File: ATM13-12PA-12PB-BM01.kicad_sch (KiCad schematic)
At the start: 1 part

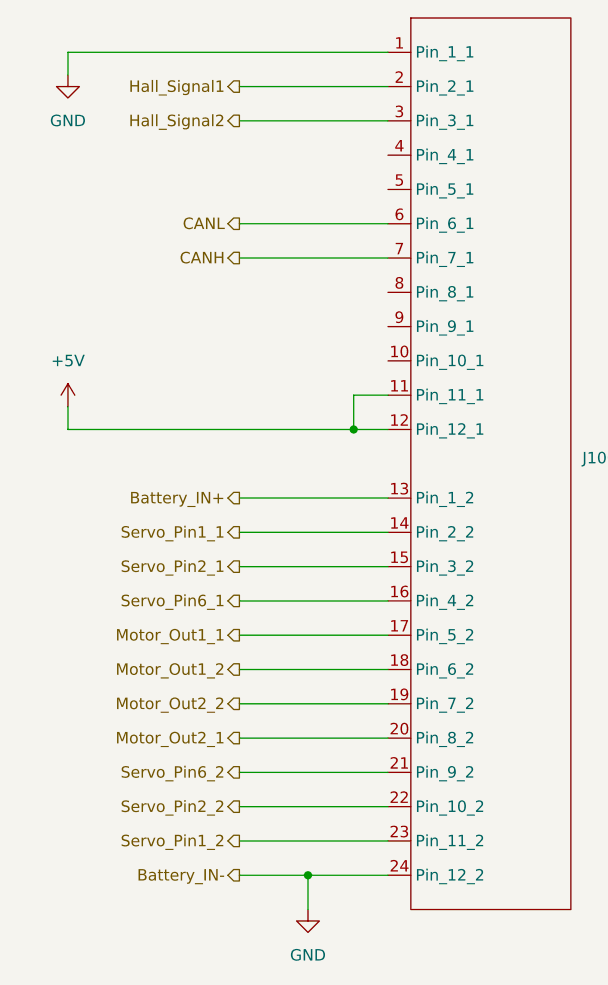
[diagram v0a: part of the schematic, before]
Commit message: Added gyro, current sense, removed servo control, added temp sense
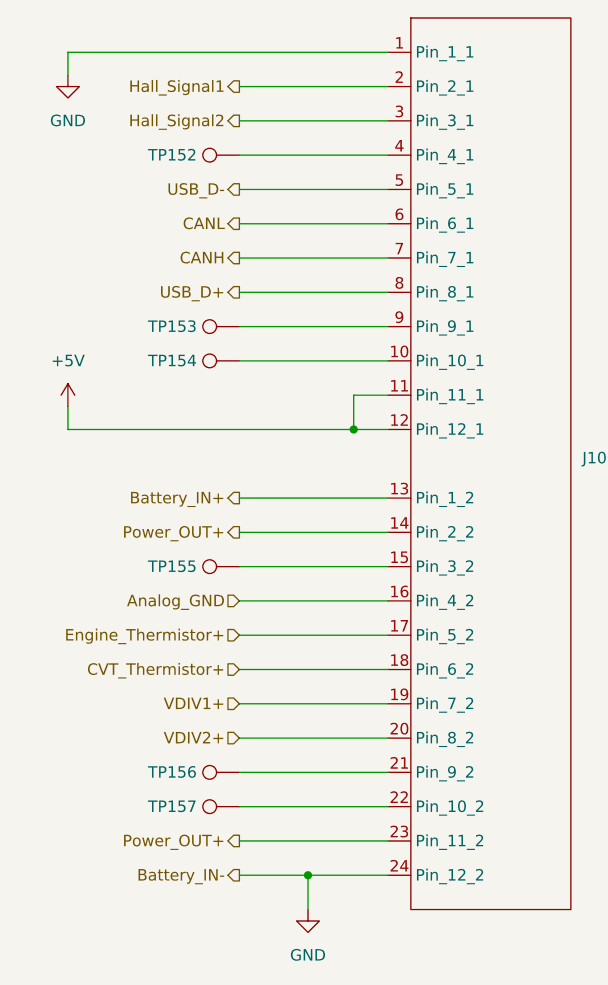
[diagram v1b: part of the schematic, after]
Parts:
- added TP152, TP153, TP154, TP155, TP156, TP157: TestPoint, TestPoint:TestPoint_Pad_D2.0mm, symbol Connector:TestPoint
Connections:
- net Servo_Pin1_2 is gone; now on net Power_OUT+: J100.23 (Pin_11_2)
- net at J100.10 (Pin_10_1): now also TP154.1
- net at J100.4 (Pin_4_1): now also TP152.1
- net USB_D-: now reaches J100.5 (Pin_5_1)
- net USB_D+: now reaches J100.8 (Pin_8_1)
- net at J100.9 (Pin_9_1): now also TP153.1
- net Motor_Out1_1 renamed Engine_Thermistor+
- net Motor_Out1_2 renamed CVT_Thermistor+
- net Motor_Out2_1 renamed VDIV2+
- net Motor_Out2_2 renamed VDIV1+
- net Servo_Pin1_1 renamed Power_OUT+
- net Servo_Pin2_1: no longer names the net of J100.15 (Pin_3_2)
- net Servo_Pin2_1: now also TP155.1
- net Servo_Pin2_2: no longer names the net of J100.22 (Pin_10_2)
- net Servo_Pin2_2: now also TP157.1
- net Servo_Pin6_1 renamed Analog_GND
- net Servo_Pin6_2: no longer names the net of J100.21 (Pin_9_2)
- net Servo_Pin6_2: now also TP156.1

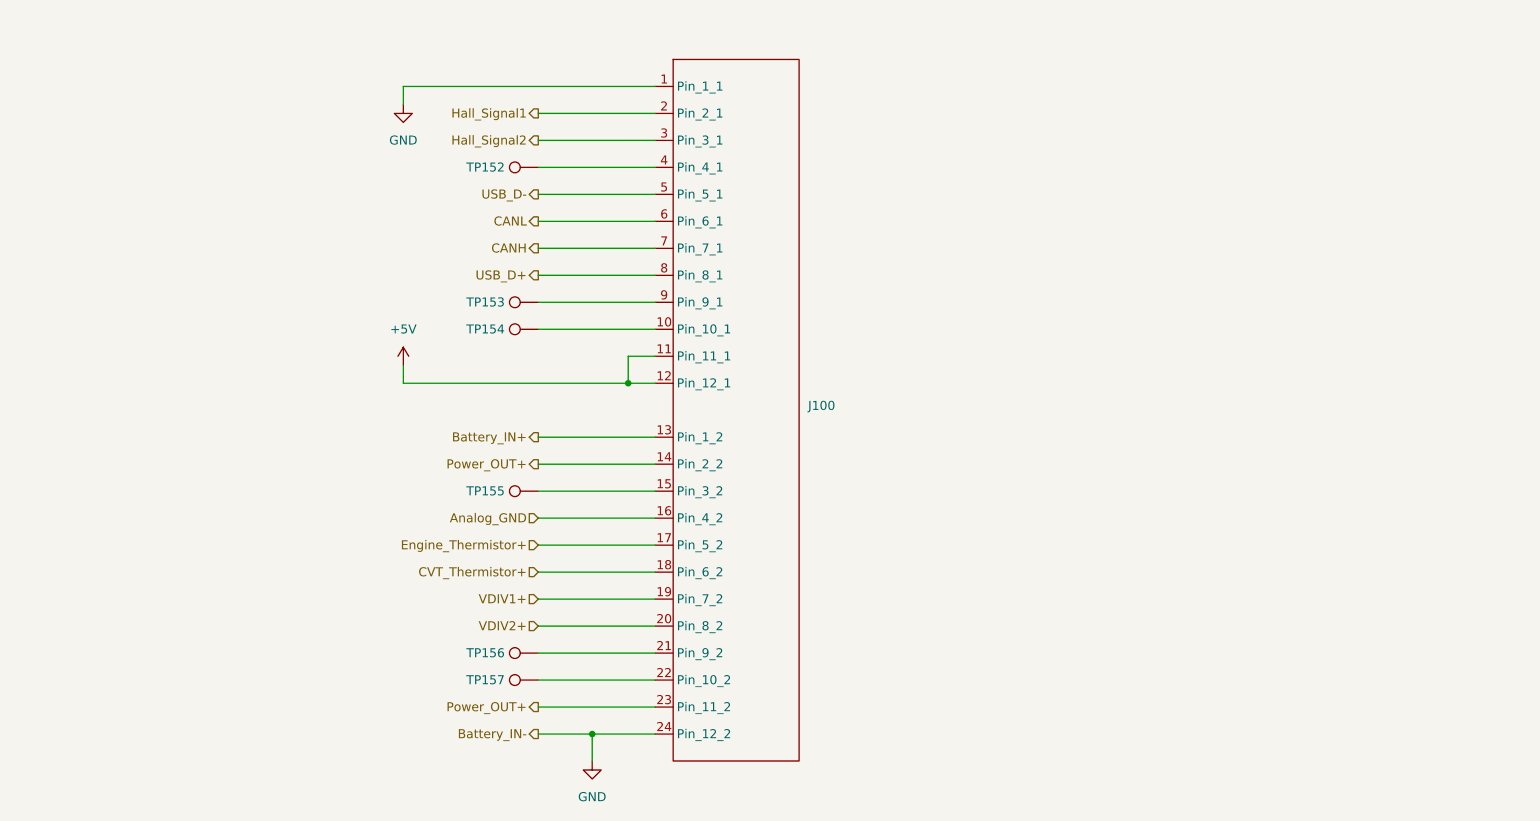
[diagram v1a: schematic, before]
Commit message: finished up schematic, added magnetic sensor, cleaned up pins, etc.
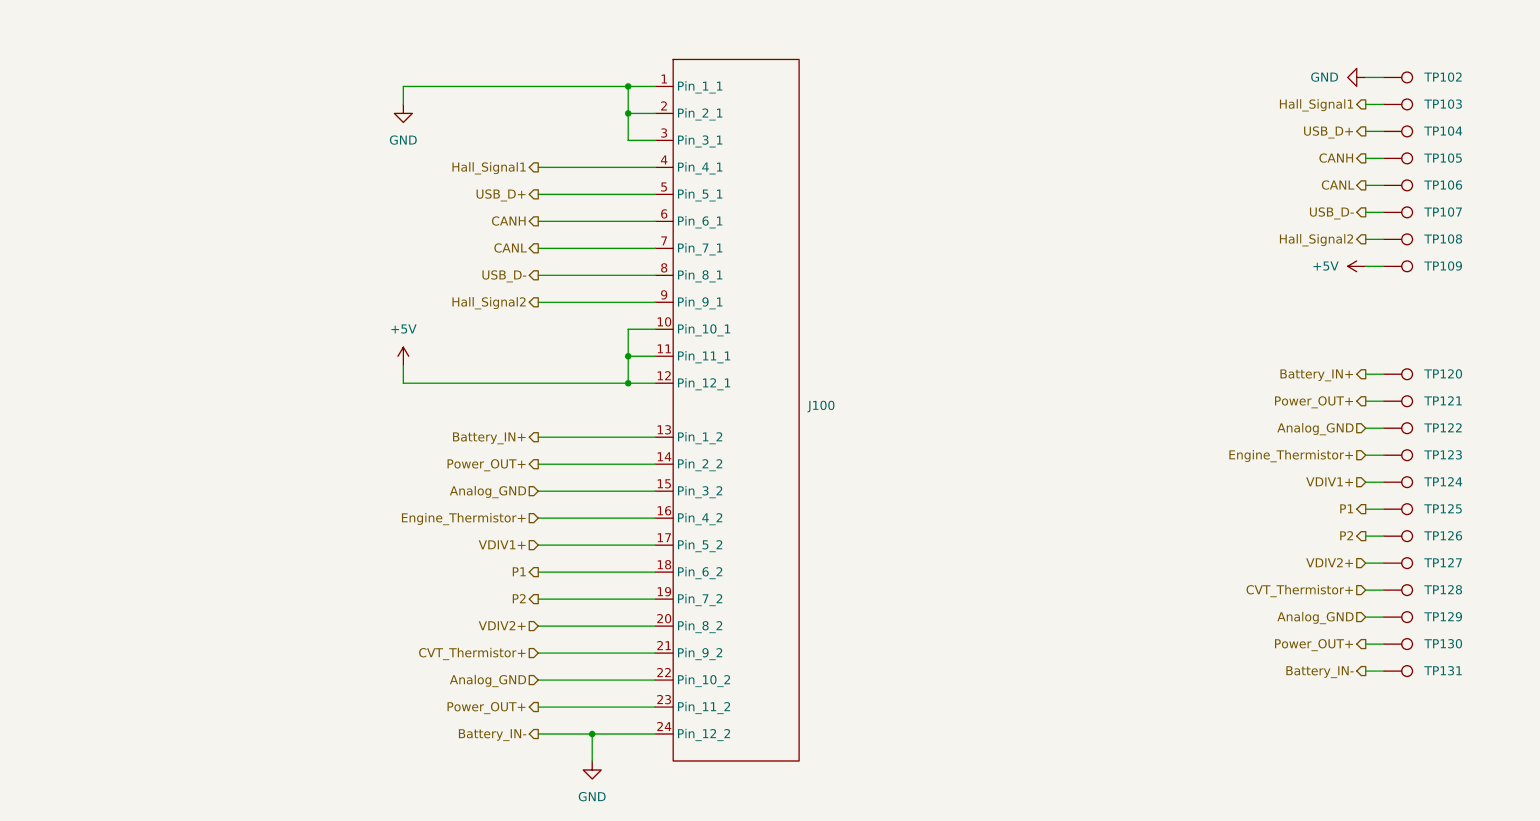
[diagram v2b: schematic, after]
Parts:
- removed TP152, TP153, TP154, TP155, TP156, TP157: TestPoint, TestPoint:TestPoint_Pad_D2.0mm, symbol Connector:TestPoint
- added TP102, TP103, TP104, TP105, TP106, TP107, TP108, TP109, TP120, TP121, TP122, TP123, TP124, TP125, TP126, TP127, TP128, TP129, TP130, TP131: TestPoint, TestPoint:TestPoint_Pad_D1.0mm, symbol Connector:TestPoint
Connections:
- net +5V: now also J100.10 (Pin_10_1), TP109.1
- net Analog_GND: now also J100.15 (Pin_3_2), J100.22 (Pin_10_2), TP122.1, TP129.1; no longer J100.16 (Pin_4_2)
- net Battery_IN+: now also TP120.1
- net CANH: now also J100.6 (Pin_6_1), TP105.1; no longer J100.7 (Pin_7_1)
- net CANL: now also J100.7 (Pin_7_1), TP106.1; no longer J100.6 (Pin_6_1)
- net CVT_Thermistor+: now also J100.21 (Pin_9_2), TP128.1; no longer J100.18 (Pin_6_2)
- net Engine_Thermistor+: now also J100.16 (Pin_4_2), TP123.1; no longer J100.17 (Pin_5_2)
- net GND: now also J100.2 (Pin_2_1), J100.3 (Pin_3_1), TP102.1, TP131.1
- net Hall_Signal1: now also J100.4 (Pin_4_1), TP103.1; no longer J100.2 (Pin_2_1)
- net Hall_Signal2: now also J100.9 (Pin_9_1), TP108.1; no longer J100.3 (Pin_3_1)
- net Power_OUT+: now also TP121.1, TP130.1
- net USB_D+: now also J100.5 (Pin_5_1), TP104.1; no longer J100.8 (Pin_8_1)
- net USB_D-: now also J100.8 (Pin_8_1), TP107.1; no longer J100.5 (Pin_5_1)
- net VDIV1+: now also J100.17 (Pin_5_2), TP124.1; no longer J100.19 (Pin_7_2)
- net VDIV2+: now also TP127.1
- new net P1: J100.18 (Pin_6_2), TP125.1
- new net P2: J100.19 (Pin_7_2), TP126.1

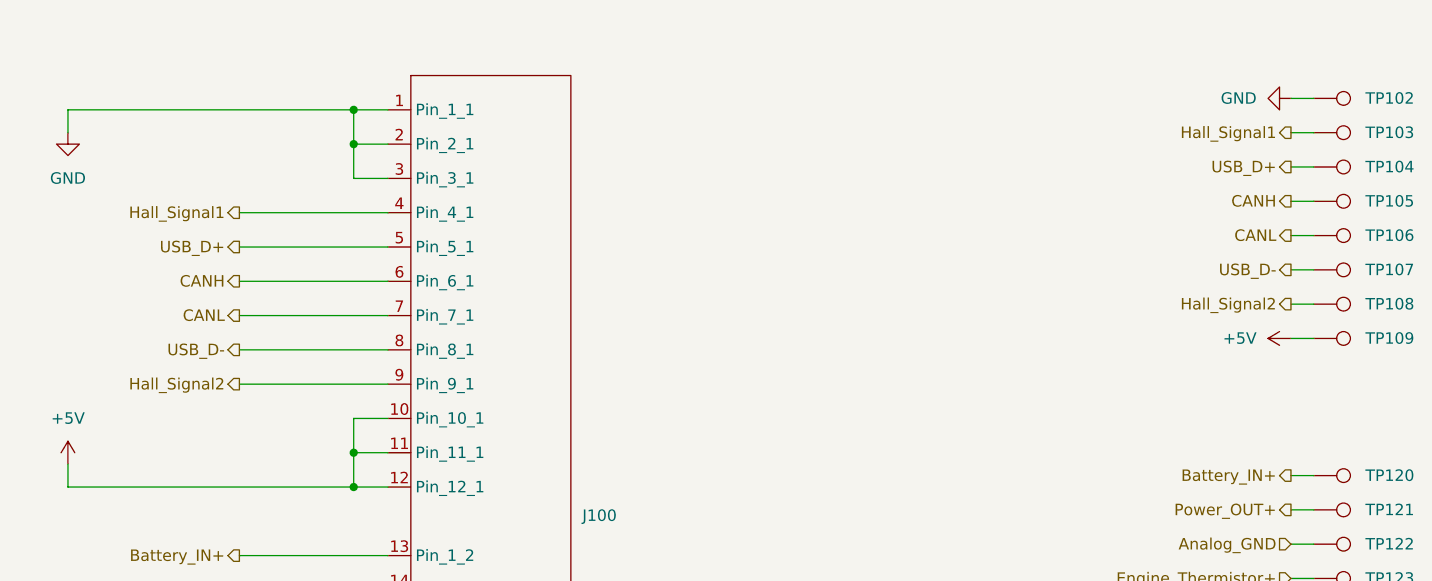
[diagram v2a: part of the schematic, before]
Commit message: final route. Needs revision and check of via placement.
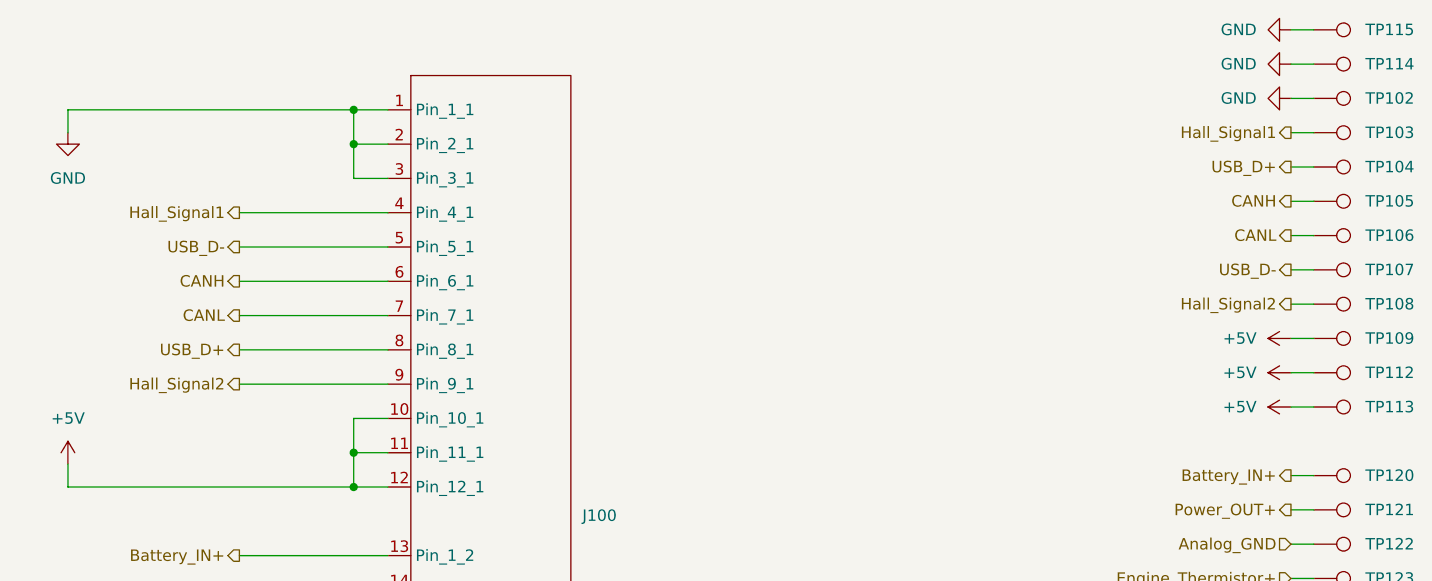
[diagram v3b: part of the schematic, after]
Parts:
- added TP112, TP113, TP114, TP115: TestPoint, TestPoint:TestPoint_Pad_D1.0mm, symbol Connector:TestPoint
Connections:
- net +5V: now also TP112.1, TP113.1
- net GND: now also TP114.1, TP115.1
- net USB_D+: now also J100.8 (Pin_8_1); no longer J100.5 (Pin_5_1)
- net USB_D-: now also J100.5 (Pin_5_1); no longer J100.8 (Pin_8_1)
